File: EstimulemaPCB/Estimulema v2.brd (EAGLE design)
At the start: 151 x 162 mm, 159 parts, among them IC3 74AC14N, IC4 ISO7240S, J1 JUMPERS12MM, J2 J15MM, J3 J_7MM, J4 JUMPERS5MM, J5 JUMPERS7MM, J6 J7MM, K2 HC-06, Q17 TIP48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

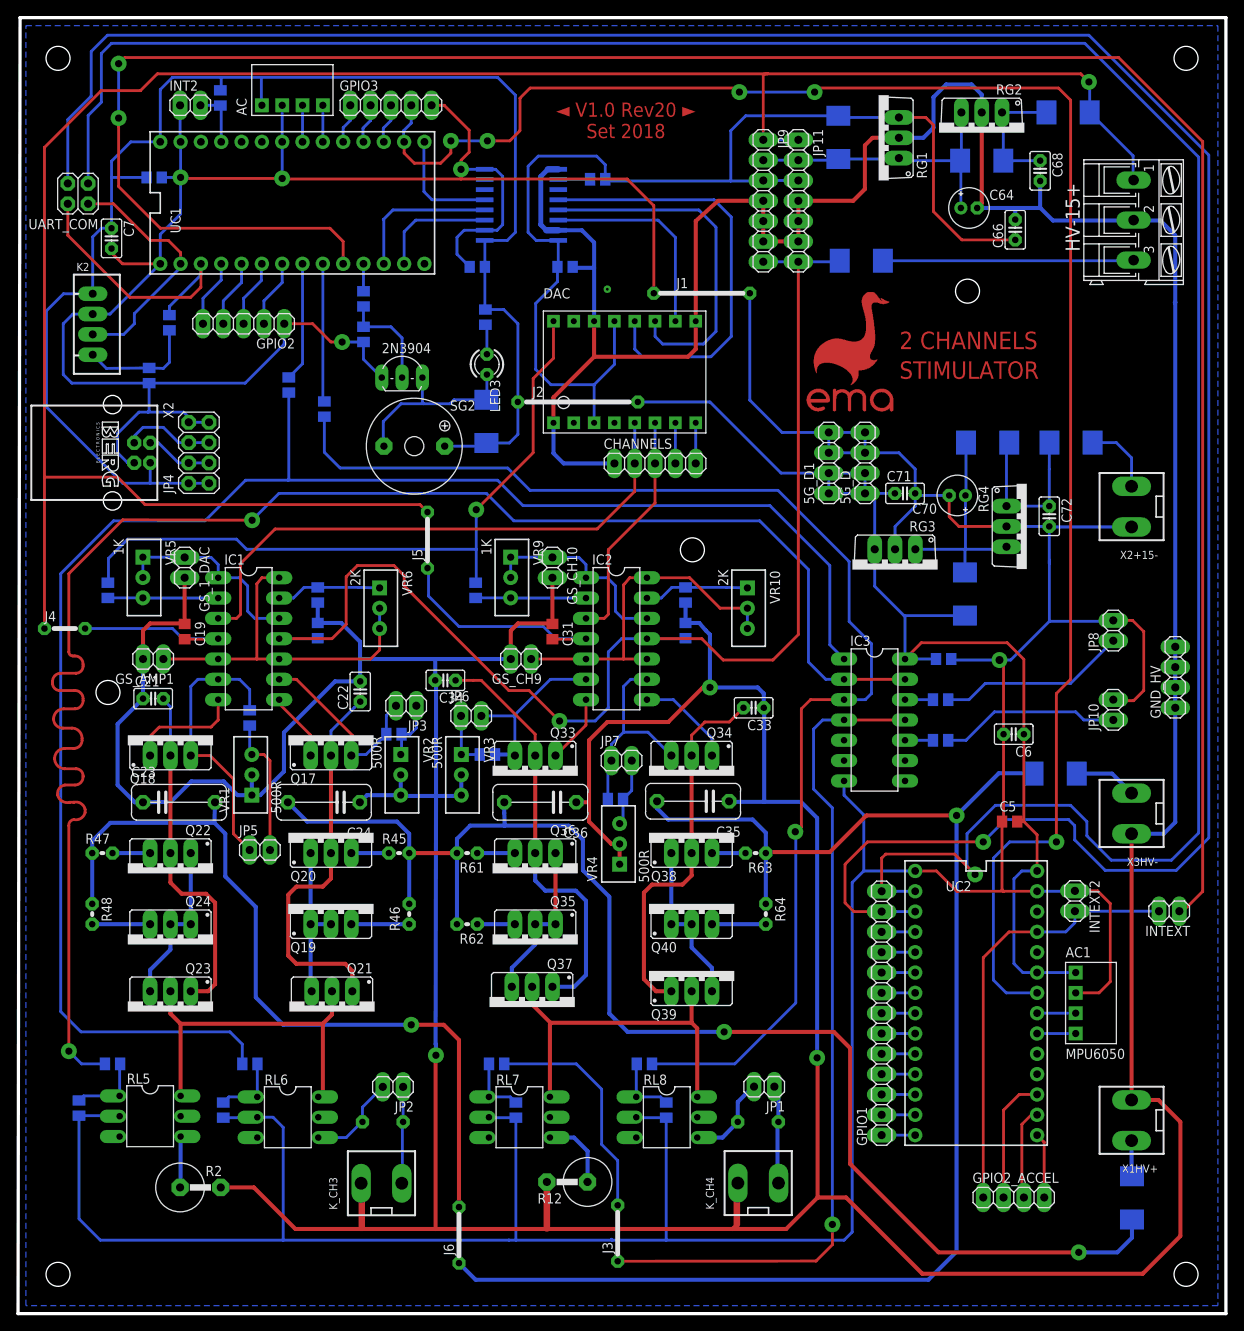
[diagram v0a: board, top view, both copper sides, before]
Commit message: correciones de errores captura de acelerometro en secion de entrenamiento
se corrigieron errores de generacion de archivo y parada de captura de datos
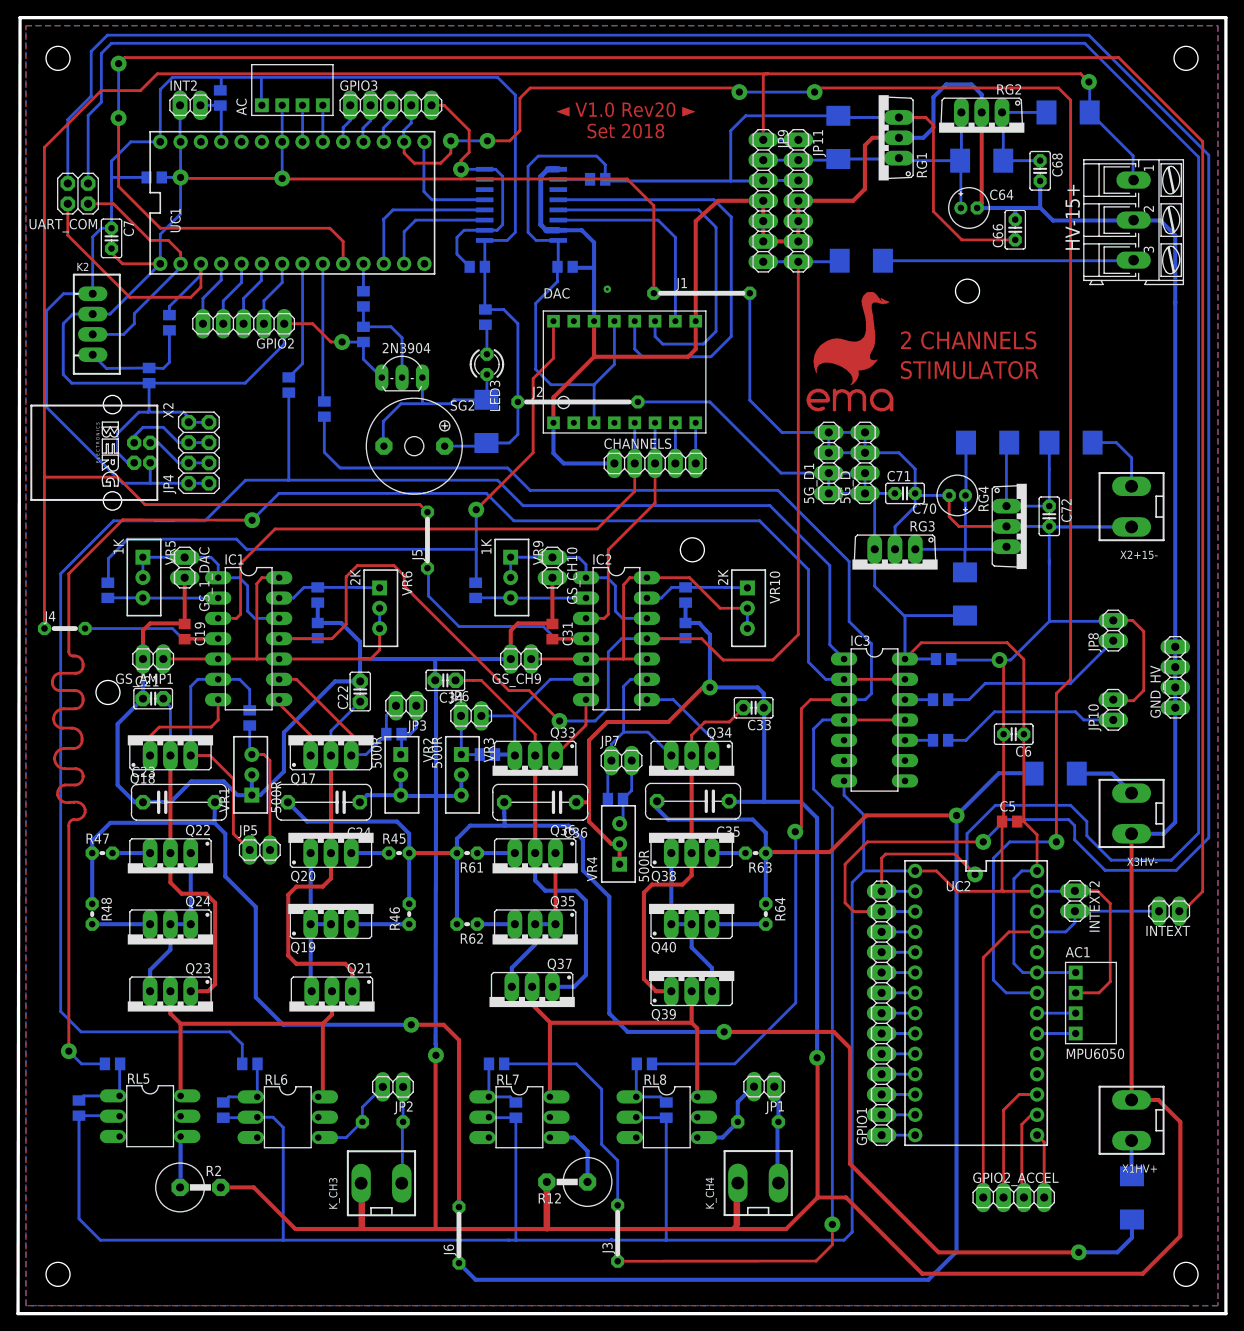
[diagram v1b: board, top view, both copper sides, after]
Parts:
- X1HV+, X3HV-: value (none) -> CONECTOR_5.08
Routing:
- added copper zone on layer 1, net N$41
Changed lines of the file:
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@@
 <drawing>
 <settings>
-<setting alwaysvectorfont="no"/>
+<setting alwaysvectorfont="yes"/>
 <setting verticaltext="up"/>
 </settings>
@@
 </layers>
 <board>
-<fusionsync huburn="a.cGVyc29uYWw6dWUyOGM0MjA1" projecturn="a.cGVyc29uYWw6dWUyOGM0MjA1IzIwMTgxMDE3MTU1MjAxMDAx" f3durn="urn:adsk.wipprod:dm.lineage:YrWJLHFmSrSkXG5gXTeEaQ" pcbguid="cdcc5b57-a677-4e81-ab74-f5285da69468" lastpulledtime="" lastsyncedchangeguid="fa68131f-7e54-75a4-66c9-be9c0c666760"/>
+<fusionsync huburn="a.cGVyc29uYWw6dWUyOGM0MjA1" projecturn="a.cGVyc29uYWw6dWUyOGM0MjA1IzIwMTgxMDE3MTU1MjAxMDAx" f3durn="urn:adsk.wipprod:dm.lineage:YrWJLHFmSrSkXG5gXTeEaQ" pcbguid="cdcc5b57-a677-4e81-ab74-f5285da69468" lastpulledtime="" lastsyncedchangeguid="35dbb72c-dffa-3be6-3d12-e2b4057d6218"/>
 <plain>
 <wire x1="1.016" y1="50" x2="152" y2="50" width="0.4064" layer="20"/>
@@
 <text x="38.6334" y="65.1764" size="1.27" layer="26" font="vector">GND</text>
 <text x="88.1888" y="181.0512" size="1.27" layer="26" font="vector">-15</text>
-<polygon width="0.4064" layer="29" pour="cutout">
-<vertex x="2" y="211"/>
-<vertex x="151" y="211"/>
-<vertex x="151" y="51"/>
-<vertex x="147" y="51"/>
-<vertex x="2" y="51"/>
-<vertex x="2" y="58"/>
-</polygon>
 </plain>
 <attributes>
@@
 <attribute name="VALUE" x="35.941" y="134.112" size="1.27" layer="28" rot="MR90"/>
 </element>
-<element name="C22" library="7DI Library" library_urn="urn:adsk.eagle:library:1229688" package="CAP_CER_2,54-5X5" package3d_urn="urn:adsk.eagle:package:1281700/3" value="100nf" x="43.7896" y="127.762" smashed="yes" rot="R90">
+<element name="C22" library="7DI Library" library_urn="urn:adsk.eagle:library:1229688" package="CAP_CER_2,54-5X5" package3d_urn="urn:adsk.eagle:package:1281700/4" value="100nf" x="43.7896" y="127.762" smashed="yes" rot="R90">
 <attribute name="NAME" x="42.2656" y="125.476" size="1.27" layer="25" ratio="10" rot="R90"/>
 <attribute name="VALUE" x="46.5836" y="125.476" size="1.27" layer="27" ratio="10" rot="R90"/>
 </element>
-<element name="C21" library="7DI Library" library_urn="urn:adsk.eagle:library:1229688" package="CAP_CER_2,54-5X5" package3d_urn="urn:adsk.eagle:package:1281700/3" value="100nf" x="17.907" y="126.873" smashed="yes">
+<element name="C21" library="7DI Library" library_urn="urn:adsk.eagle:library:1229688" package="CAP_CER_2,54-5X5" package3d_urn="urn:adsk.eagle:package:1281700/4" value="100nf" x="17.907" y="126.873" smashed="yes">
 <attribute name="NAME" x="15.621" y="128.397" size="1.27" layer="25" ratio="10"/>
 <attribute name="VALUE" x="15.621" y="124.079" size="1.27" layer="27" ratio="10"/>
@@
 <attribute name="VALUE" x="81.915" y="134.112" size="1.27" layer="28" rot="MR90"/>
 </element>
-<element name="C34" library="7DI Library" library_urn="urn:adsk.eagle:library:1229688" package="CAP_CER_2,54-5X5" package3d_urn="urn:adsk.eagle:package:1281700/3" value="100nf" x="54.4322" y="129.159" smashed="yes" rot="R180">
+<element name="C34" library="7DI Library" library_urn="urn:adsk.eagle:library:1229688" package="CAP_CER_2,54-5X5" package3d_urn="urn:adsk.eagle:package:1281700/4" value="100nf" x="54.4322" y="129.159" smashed="yes" rot="R180">
 <attribute name="NAME" x="56.7182" y="127.635" size="1.27" layer="25" ratio="10" rot="R180"/>
 <attribute name="VALUE" x="56.7182" y="131.953" size="1.27" layer="27" ratio="10" rot="R180"/>
 </element>
-<element name="C33" library="7DI Library" library_urn="urn:adsk.eagle:library:1229688" package="CAP_CER_2,54-5X5" package3d_urn="urn:adsk.eagle:package:1281700/3" value="100nf" x="92.964" y="125.73" smashed="yes" rot="R180">
+<element name="C33" library="7DI Library" library_urn="urn:adsk.eagle:library:1229688" package="CAP_CER_2,54-5X5" package3d_urn="urn:adsk.eagle:package:1281700/4" value="100nf" x="92.964" y="125.73" smashed="yes" rot="R180">
 <attribute name="NAME" x="95.25" y="124.206" size="1.27" layer="25" ratio="10" rot="R180"/>
 <attribute name="VALUE" x="95.25" y="128.524" size="1.27" layer="27" ratio="10" rot="R180"/>
@@
 <attribute name="VALUE" x="34.0995" y="76.962" size="1.27" layer="27" ratio="10" rot="R270"/>
 </element>
-<element name="K_CH3" library="7DI Library" library_urn="urn:adsk.eagle:library:1229688" package="CONECTOR_X2_5.08" package3d_urn="urn:adsk.eagle:package:1393551/4" value="CONECTOR_5.08" x="46.4439" y="66.294" smashed="yes">
+<element name="K_CH3" library="7DI Library" library_urn="urn:adsk.eagle:library:1229688" package="CONECTOR_X2_5.08" package3d_urn="urn:adsk.eagle:package:1393551/5" value="CONECTOR_5.08" x="46.4439" y="66.294" smashed="yes">
 <attribute name="NAME" x="40.9189" y="62.984" size="1.016" layer="25" ratio="10" rot="R90"/>
 <attribute name="VALUE" x="43.1414" y="71.4565" size="1.016" layer="27" ratio="10"/>
@@
 <attribute name="VALUE" x="81.4705" y="76.962" size="1.27" layer="27" ratio="10" rot="R270"/>
 </element>
-<element name="K_CH4" library="7DI Library" library_urn="urn:adsk.eagle:library:1229688" package="CONECTOR_X2_5.08" package3d_urn="urn:adsk.eagle:package:1393551/4" value="CONECTOR_5.08" x="93.5355" y="66.3194" smashed="yes">
+<element name="K_CH4" library="7DI Library" library_urn="urn:adsk.eagle:library:1229688" package="CONECTOR_X2_5.08" package3d_urn="urn:adsk.eagle:package:1393551/5" value="CONECTOR_5.08" x="93.5355" y="66.3194" smashed="yes">
 <attribute name="NAME" x="88.0105" y="63.0094" size="1.016" layer="25" ratio="10" rot="R90"/>
 <attribute name="VALUE" x="90.233" y="71.4819" size="1.016" layer="27" ratio="10"/>
@@
 <attribute name="VALUE" x="115.062" y="124.206" size="1.27" layer="28" rot="MR180"/>
 </element>
-<element name="X1HV+" library="7DI Library" library_urn="urn:adsk.eagle:library:1229688" package="CONECTOR_X2_5.08" package3d_urn="urn:adsk.eagle:package:1393551/4" value="" x="140.208" y="74.168" smashed="yes" rot="R90">
+<element name="X1HV+" library="7DI Library" library_urn="urn:adsk.eagle:library:1229688" package="CONECTOR_X2_5.08" package3d_urn="urn:adsk.eagle:package:1393551/5" value="CONECTOR_5.08" x="140.208" y="74.168" smashed="yes" rot="R90">
 <attribute name="NAME" x="143.518" y="68.643" size="1.016" layer="25" ratio="10" rot="R180"/>
 <attribute name="VALUE" x="135.0455" y="70.8655" size="1.016" layer="27" ratio="10" rot="R90"/>
 </element>
-<element name="X3HV-" library="7DI Library" library_urn="urn:adsk.eagle:library:1229688" package="CONECTOR_X2_5.08" package3d_urn="urn:adsk.eagle:package:1393551/4" value="" x="140.208" y="112.522" smashed="yes" rot="R90">
+<element name="X3HV-" library="7DI Library" library_urn="urn:adsk.eagle:library:1229688" package="CONECTOR_X2_5.08" package3d_urn="urn:adsk.eagle:package:1393551/5" value="CONECTOR_5.08" x="140.208" y="112.522" smashed="yes" rot="R90">
 <attribute name="NAME" x="143.518" y="106.997" size="1.016" layer="25" ratio="10" rot="R180"/>
 <attribute name="VALUE" x="135.0455" y="109.2195" size="1.016" layer="27" ratio="10" rot="R90"/>
 </element>
-<element name="X2+15-" library="7DI Library" library_urn="urn:adsk.eagle:library:1229688" package="CONECTOR_X2_5.08" package3d_urn="urn:adsk.eagle:package:1393551/4" value="CONECTOR_5.08" x="140.208" y="150.876" smashed="yes" rot="R90">
+<element name="X2+15-" library="7DI Library" library_urn="urn:adsk.eagle:library:1229688" package="CONECTOR_X2_5.08" package3d_urn="urn:adsk.eagle:package:1393551/5" value="CONECTOR_5.08" x="140.208" y="150.876" smashed="yes" rot="R90">
 <attribute name="NAME" x="143.518" y="145.351" size="1.016" layer="25" ratio="10" rot="R180"/>
 <attribute name="VALUE" x="135.0455" y="147.5735" size="1.016" layer="27" ratio="10" rot="R90"/>
@@
 <vertex x="2" y="51"/>
 </polygon>
+<wire x1="73.025" y1="180.721" x2="74.676" y2="178.054" width="0" layer="19" extent="16-16"/>
+<wire x1="43.9039" y1="66.294" x2="43.9801" y2="66.294" width="0" layer="19" extent="1-1"/>
+<wire x1="140.462" y1="186.69" x2="140.3985" y2="186.6392" width="0" layer="19" extent="16-16"/>
+<wire x1="90.9955" y1="66.3194" x2="90.8685" y2="66.2686" width="0" layer="19" extent="1-1"/>
 </signal>
 <signal name="N$75" class="2">
@@
 <wire x1="126.1618" y1="77.3938" x2="124.206" y2="75.438" width="0.3556" layer="1"/>
 </signal>
+<signal name="N$41">
+<polygon width="0.4064" layer="1">
+<vertex x="2" y="211"/>
+<vertex x="151" y="211"/>
+<vertex x="151" y="51"/>
+<vertex x="147" y="51"/>
+<vertex x="2" y="51"/>
+<vertex x="2" y="58"/>
+</polygon>
+</signal>
 </signals>
